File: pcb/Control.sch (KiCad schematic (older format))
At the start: 23 parts, among them SW1 Pulsador_4p, U1 ATMEGA328, U2 PCA9685, U3 FT231X, Y1 16MHz

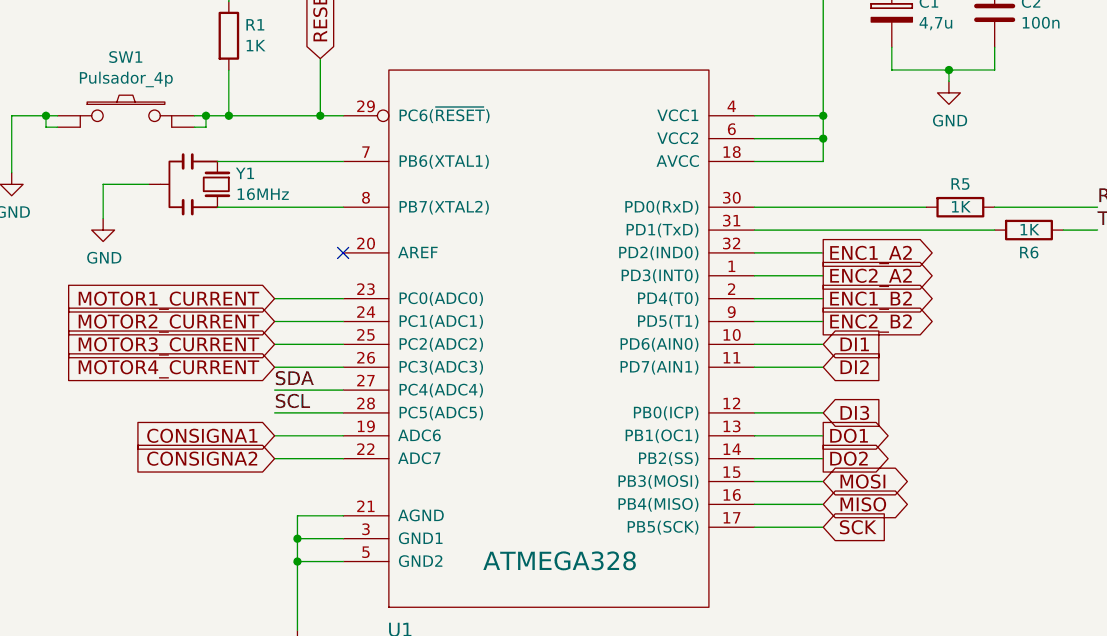
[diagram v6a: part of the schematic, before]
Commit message: se añaden optos para E/S y cristal
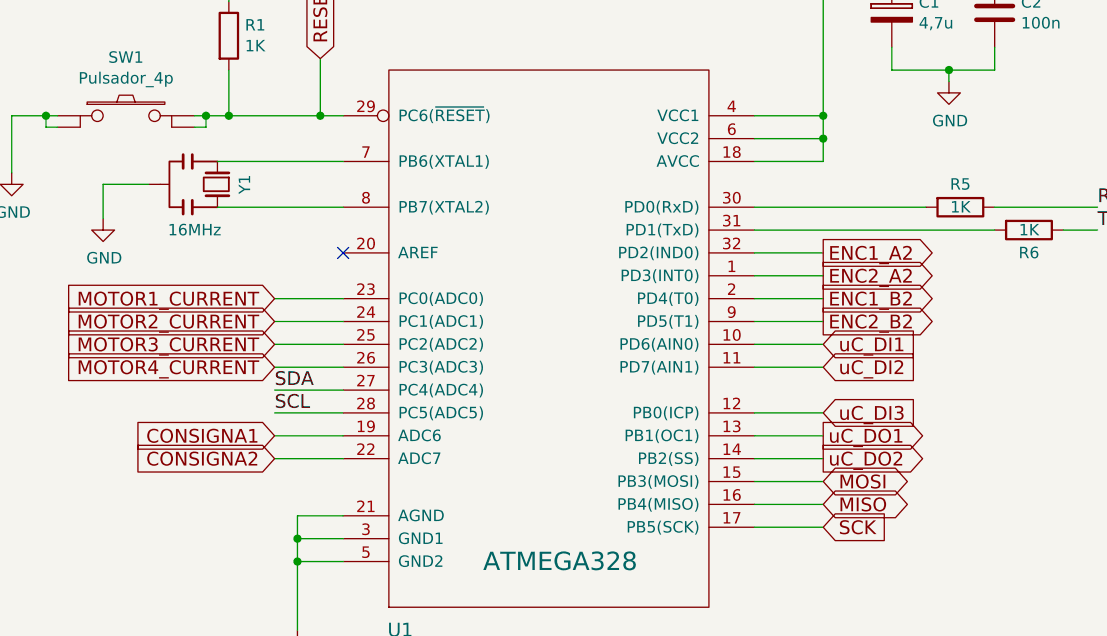
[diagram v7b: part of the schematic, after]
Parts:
- Y1: footprint (none) -> Cristal:Murata_CSTCE_V_A; Fabricante IQD FREQUENCY PRODUCTS -> Murata; Proveedor tme -> rs; Ref LF SPXO018034 -> CSTCE16M0V53-R0; Ref. Proveedor CFPS-72-16M -> 792-6524
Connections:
- net DI1 renamed uC_DI1
- net DI2 renamed uC_DI2
- net DI3 renamed uC_DI3
- net DO1 renamed uC_DO1
- net DO2 renamed uC_DO2
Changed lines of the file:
@@
 LIBS:Opamp
 LIBS:Traco
+LIBS:Optoacoplados
 LIBS:ATMEGA328_Motor_Board-cache
 EELAYER 25 0
@@
 $Descr A4 11693 8268
 encoding utf-8
-Sheet 2 6
+Sheet 2 7
 Title ""
 Date ""
@@
 U 1 1 57689A0E
 P 1600 2150
-F 0 "Y1" V 1554 2231 50  0000 L CNN
-F 1 "16MHz" V 1645 2231 50  0000 L CNN
-F 2 "" H 2030 2260 50  0001 C CNN
+F 0 "Y1" H 1600 2270 50  0000 C CNN
+F 1 "16MHz" V 1800 2050 50  0000 C CNN
+F 2 "Cristal:Murata_CSTCE_V_A" H 2030 2260 50  0001 C CNN
 F 3 "" H 2030 2260 50  0000 C CNN
-F 4 "IQD FREQUENCY PRODUCTS" V 1600 2150 60  0001 C CNN "Fabricante"
-F 5 "LF SPXO018034" V 1600 2150 60  0001 C CNN "Ref"
+F 4 "Murata" V 1600 2150 60  0001 C CNN "Fabricante"
+F 5 "CSTCE16M0V53-R0" V 1600 2150 60  0001 C CNN "Ref"
 F 6 "~" H 1600 2150 60  0001 C CNN "Potencia"
 F 7 "~" H 1600 2150 60  0001 C CNN "Tolerancia"
 F 8 "~" H 1600 2150 60  0001 C CNN "Provedor"
 F 9 "~" H 1600 2150 60  0001 C CNN "Ref_Proveedor"
-F 10 "tme" V 1600 2150 60  0001 C CNN "Proveedor"
-F 11 "CFPS-72-16M" V 1600 2150 60  0001 C CNN "Ref. Proveedor"
+F 10 "rs" V 1600 2150 60  0001 C CNN "Proveedor"
+F 11 "792-6524" V 1600 2150 60  0001 C CNN "Ref. Proveedor"
 	1    1600 2150
 	0    1    1    0
@@
 $EndComp
 Text GLabel 4250 2850 2    60   Input ~ 0
-DI1
+uC_DI1
 Text GLabel 4250 2950 2    60   Input ~ 0
-DI2
+uC_DI2
 Text GLabel 4250 3150 2    60   Input ~ 0
-DI3
+uC_DI3
 Text GLabel 4250 3250 2    60   Output ~ 0
-DO1
+uC_DO1
 Text GLabel 4250 3350 2    60   Output ~ 0
-DO2
+uC_DO2
 Wire Wire Line
 	3950 2850 4250 2850

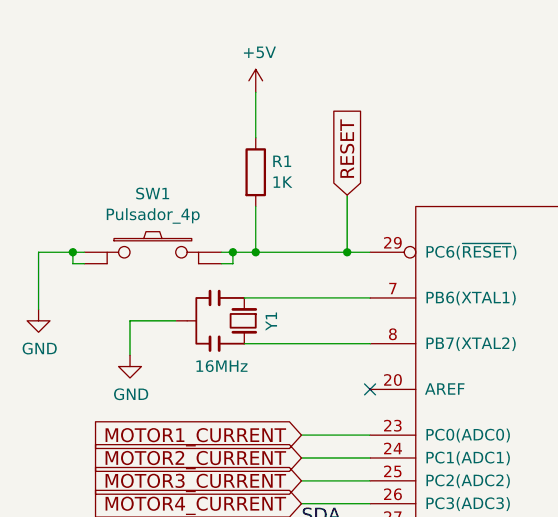
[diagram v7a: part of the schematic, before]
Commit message: finalizado el posicionado sobre la pcb
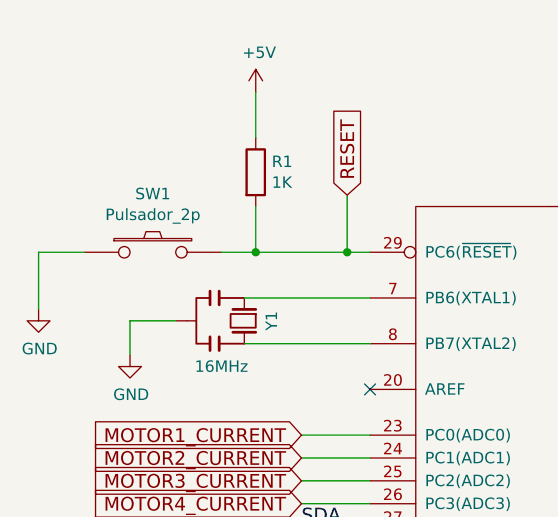
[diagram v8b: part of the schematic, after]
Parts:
- removed SW1: Pulsador_4p, Relays_and_Contacts:ALP_SKQGAKE010, symbol Pulsador_4p
- added SW1: Pulsador_2p, Relays_and_Contacts:CANAL_ELECTRONIC_DTSM-31N-B, symbol Pulsador_2p
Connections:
- net GND: now also SW1.1
- net RESET: now also SW1.2
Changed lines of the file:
@@
 Text GLabel 4250 2750 2    60   Output ~ 0
 ENC2_B2
-$Comp
-L Pulsador_4p SW1
-U 1 1 576FB09C
-P 1200 1850
-F 0 "SW1" H 1200 2105 50  0000 C CNN
-F 1 "Pulsador_4p" H 1200 2014 50  0000 C CNN
-F 2 "Relays_and_Contacts:ALP_SKQGAKE010" H 1200 1850 50  0001 C CNN
-F 3 "" H 1200 1850 50  0000 C CNN
-	1    1200 1850
-	1    0    0    -1
-$EndComp
 Connection ~ 1650 1850
-Wire Wire Line
-	1500 1900 1550 1900
-Wire Wire Line
-	1550 1900 1550 1850
-Connection ~ 1550 1850
 Wire Wire Line
 	900  1850 700  1850
@@
 	1    0    0    -1
 $EndComp
-Wire Wire Line
-	900  1900 850  1900
-Wire Wire Line
-	850  1900 850  1850
-Connection ~ 850  1850
 $Comp
 L CP C1
@@
 Wire Wire Line
 	3950 3350 4250 3350
+$Comp
+L Pulsador_2p SW1
+U 1 1 578A2160
+P 1200 1850
+F 0 "SW1" H 1200 2105 50  0000 C CNN
+F 1 "Pulsador_2p" H 1200 2014 50  0000 C CNN
+F 2 "Relays_and_Contacts:CANAL_ELECTRONIC_DTSM-31N-B" H 1200 1850 50  0001 C CNN
+F 3 "" H 1200 1850 50  0000 C CNN
+F 4 "CANAL ELECTRONIC" H 1200 1850 60  0001 C CNN "Fabricante"
+F 5 "DTSM31NB" H 1200 1850 60  0001 C CNN "Ref"
+F 6 "~" H 1200 1850 60  0001 C CNN "Potencia"
+F 7 "~" H 1200 1850 60  0001 C CNN "Tolerancia"
+F 8 "tme" H 1200 1850 60  0001 C CNN "Provedor"
+F 9 "DTSM-31N-B" H 1200 1850 60  0001 C CNN "Ref_Proveedor"
+	1    1200 1850
+	1    0    0    -1
+$EndComp
 $EndSCHEMATC
